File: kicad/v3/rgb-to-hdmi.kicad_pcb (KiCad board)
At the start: 2 copper layers, 65 x 30 mm, 30 parts, among them P1 CONN_02X20, P2 CONN_01X03, P3 CONN_01X06, P4 CONN_01X02, P5 CONN_01X06, P6 CONN_01X02, P7 Conn_01x01, SW1 SW_PUSH, SW2 SW_PUSH, SW3 SW_PUSH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

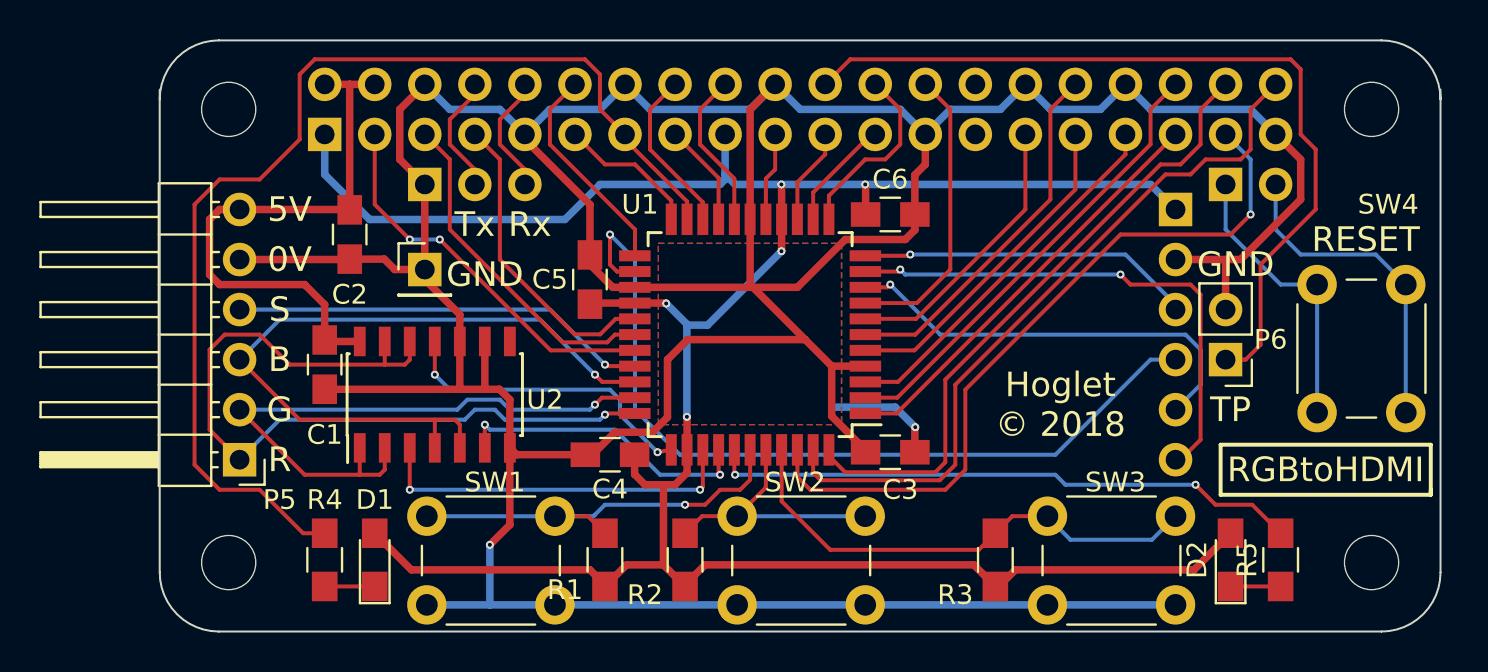
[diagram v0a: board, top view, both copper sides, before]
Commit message: KiCad: corrected via size, cleaned up silk screen
Change-Id: Icce07a46245585d3c723be4bf0025df466743eb7
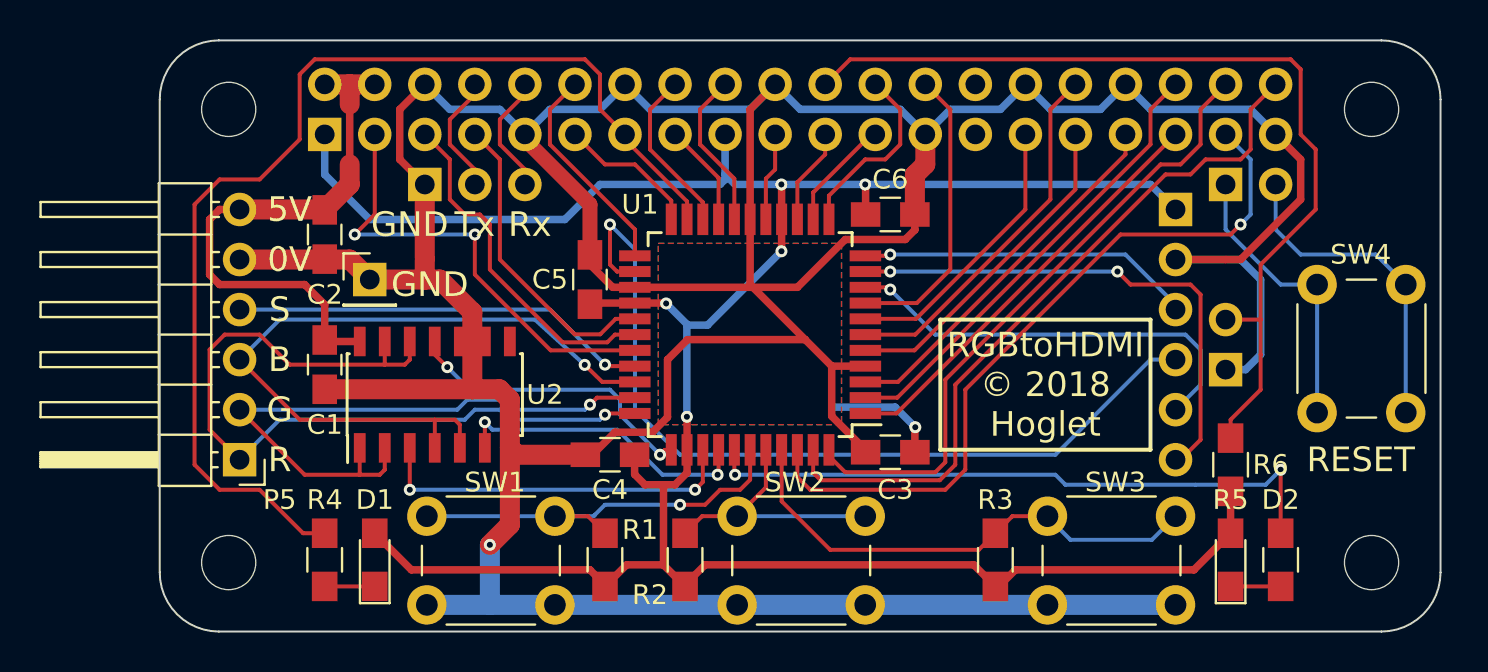
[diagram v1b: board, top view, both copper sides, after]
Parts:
- added R6: 10K, Resistors_SMD:R_0805_HandSoldering, F.Cu at (66.8, 46.0)
- P6: footprint Pin_Headers:Pin_Header_Straight_1x02_Pitch2.54mm -> Pin_Headers:Pin_Header_Angled_1x02_Pitch2.54mm; moved to B.Cu
- moved P7 2.84 mm to (23.2, 36.6)
- moved C2 1.27 mm to (20.9, 34.4)
- moved P6 0.51 mm to (66.6, 41.2), turned to 0 degrees
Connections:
- P6 pad 1: /GPIO25 -> GND
- P6 pad 2: GND -> /GPIO25
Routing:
- net GND: track 227.3 -> 238.1 mm
- net /GPIO25: track 42.4 -> 47.5 mm
- net /GPIO2: track 19.8 -> 23.3 mm
- net /LED: track 30.2 -> 32.7 mm
- net /3V3: track 137.7 -> 139.8 mm
- net /TDO: track 42.7 -> 43.7 mm
- net VCC: track 29.2 -> 28.5 mm
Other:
- outline, holes or cut-outs redrawn
- net class Default: via_dia 0.4064 -> 0.6096; via_drill 0.2032 -> 0.3048
- net class Power: via_dia 0.4064 -> 0.6096; via_drill 0.2032 -> 0.3048
- rule trace_min: 0.1524 -> 0.2032
- rule via_min_drill: 0.2032 -> 0.3048
- rule via_min_size: 0.4064 -> 0.6096
- board text added: "DEBUG"
- board text added: "LINK"
- board text added: "RGBtoHDMI © 2018 Hoglet"
- board text removed: "Hoglet © 2018"
- board text removed: "RGBtoHDMI"
- board text removed: "TP"

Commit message: KiCad: removed SW2/3 passthrough, use gpio 19/26 instead
Change-Id: I88240f36d608d24969d40a8aa7c47a878a85b3d9
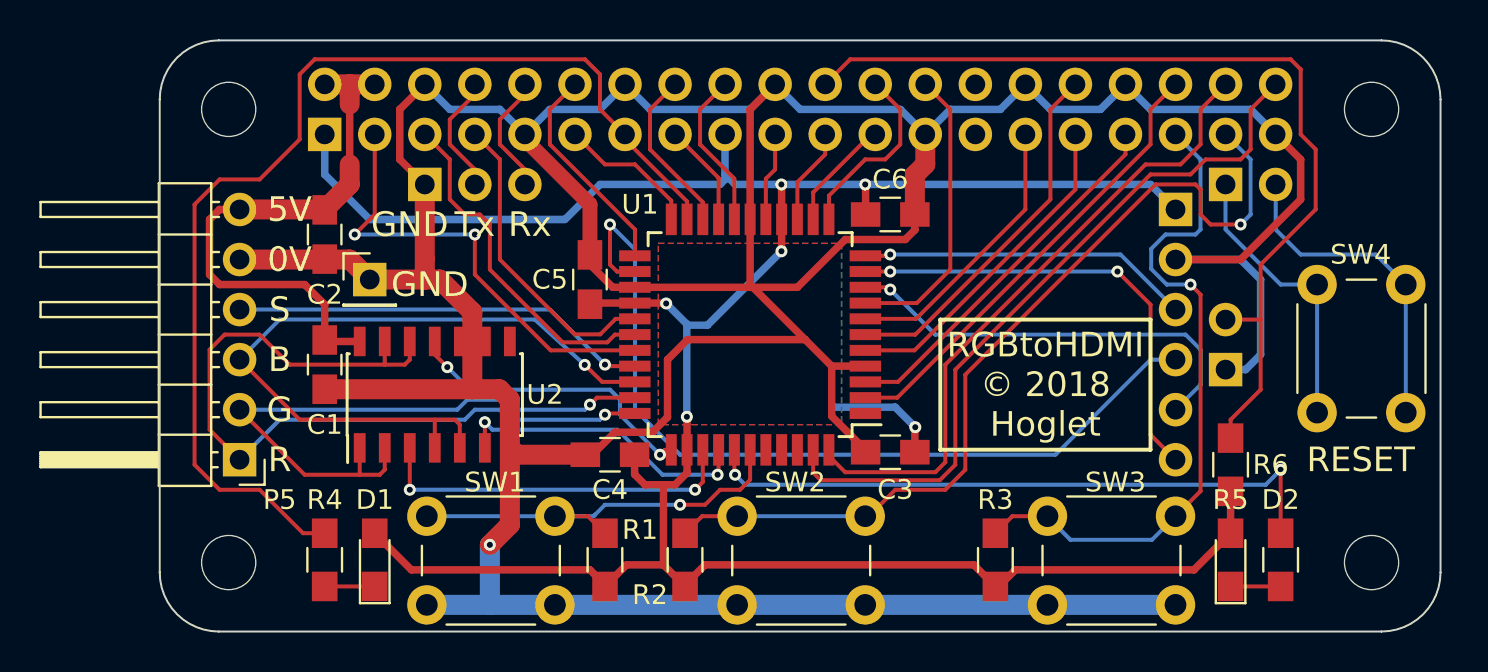
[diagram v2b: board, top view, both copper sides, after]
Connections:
- R2 pad 2: /SW2 -> /GPIO26
- R3 pad 2: /SW3 -> /GPIO19
- SW2 pad 2: /SW2 -> /GPIO26
- SW3 pad 2: /SW3 -> /GPIO19
- U1 pad 1: /GPIO19 -> (no net)
- U1 pad 40: /SW2 -> (no net)
- U1 pad 41: /SW3 -> (no net)
- U1 pad 42: /GPIO26 -> (no net)
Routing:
- net /SW3: track 25.3 -> 0.00 mm
- net /SW2: track 13.5 -> 0.00 mm
- net /GPIO19: track 21.6 -> 34.6 mm, vias 0 -> 1
- net /GPIO26: track 37.4 -> 45.2 mm
- net /TMS: track 26.7 -> 24.0 mm

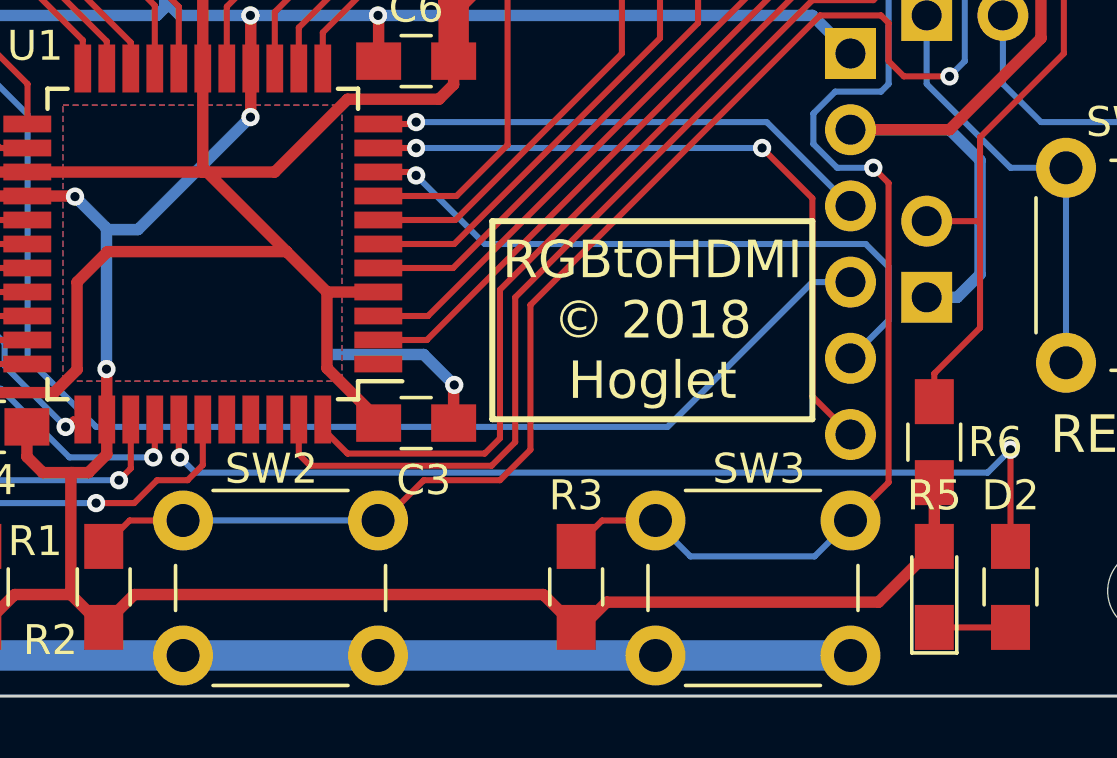
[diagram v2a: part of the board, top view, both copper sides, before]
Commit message: KiCad and CPLD: final small changes to bring SW2/3/link inputs and LED1 output to CPLD (unused)
Change-Id: I054dcab88885547d6ceb07bc2759daf81372ef52
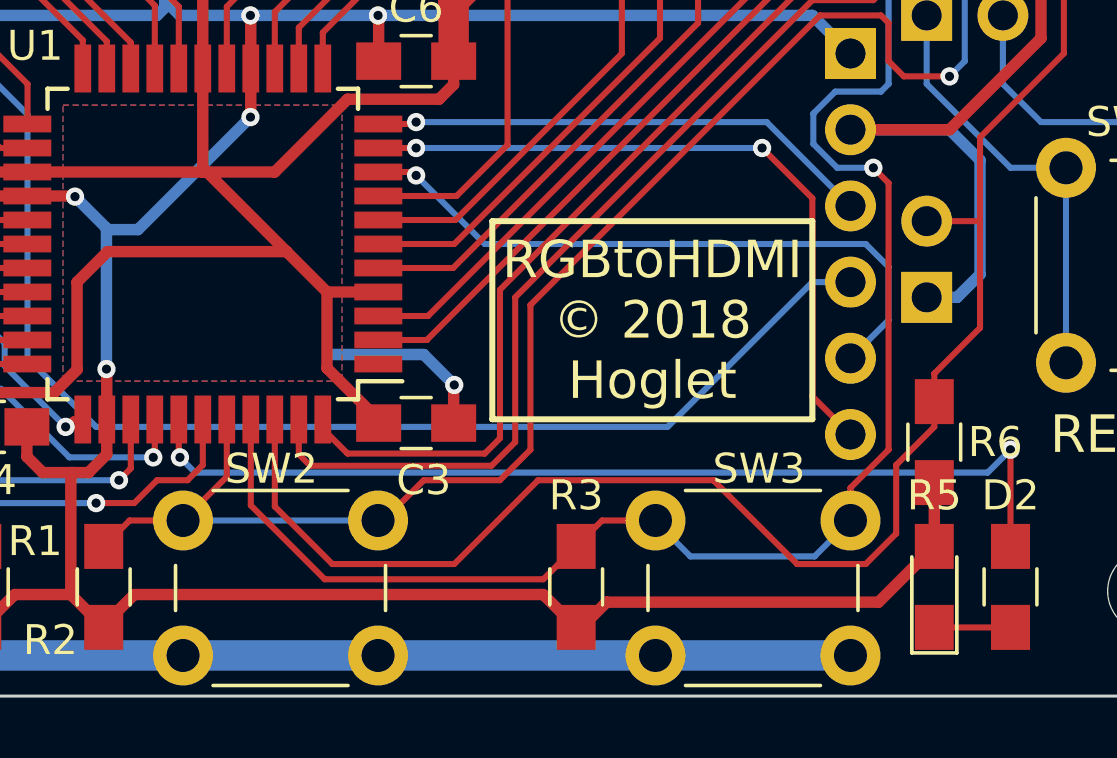
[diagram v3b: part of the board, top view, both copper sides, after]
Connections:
- U1 pad 40: (no net) -> /GPIO26
- U1 pad 41: (no net) -> /GPIO19
- U1 pad 42: (no net) -> /GPIO25
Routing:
- net /GPIO25: track 47.5 -> 79.5 mm
- net /GPIO19: track 34.6 -> 49.8 mm
- net /GPIO26: track 45.2 -> 49.2 mm
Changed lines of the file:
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@@
 (kicad_pcb (version 4) (host pcbnew 4.0.7-e2-6376~58~ubuntu16.04.1)
   (general
-    (links 109)
+    (links 112)
     (no_connects 0)
     (area 12.449999 24.449999 77.550001 54.550001)
     (thickness 1.6)
     (drawings 49)
-    (tracks 513)
+    (tracks 530)
     (zones 0)
     (modules 31)
@@
     (pad 39 smd rect (at 0 -5.85 270) (size 1.6 0.56) (layers F.Cu F.Paste F.Mask)
       (net 39 /SW1))
-    (pad 40 smd rect (at -0.8 -5.85 270) (size 1.6 0.56) (layers F.Cu F.Paste F.Mask))
-    (pad 41 smd rect (at -1.6 -5.85 270) (size 1.6 0.56) (layers F.Cu F.Paste F.Mask))
-    (pad 42 smd rect (at -2.4 -5.85 270) (size 1.6 0.56) (layers F.Cu F.Paste F.Mask))
+    (pad 40 smd rect (at -0.8 -5.85 270) (size 1.6 0.56) (layers F.Cu F.Paste F.Mask)
+      (net 26 /GPIO26))
+    (pad 41 smd rect (at -1.6 -5.85 270) (size 1.6 0.56) (layers F.Cu F.Paste F.Mask)
+      (net 24 /GPIO19))
+    (pad 42 smd rect (at -2.4 -5.85 270) (size 1.6 0.56) (layers F.Cu F.Paste F.Mask)
+      (net 46 /GPIO25))
     (pad 43 smd rect (at -3.2 -5.85 270) (size 1.6 0.56) (layers F.Cu F.Paste F.Mask)
       (net 28 /GPIO21))
@@
   (segment (start 49.968 41.83096) (end 61.512 30.28696) (width 0.2032) (layer F.Cu) (net 23))
   (segment (start 61.512 30.28696) (end 61.512 29.27096) (width 0.2032) (layer F.Cu) (net 23) (status 20))
+  (segment (start 64.052 48.64696) (end 64.052 47.55896) (width 0.2032) (layer F.Cu) (net 24) (status 10))
+  (segment (start 64.052 47.55896) (end 65.322 46.28896) (width 0.2032) (layer F.Cu) (net 24))
+  (segment (start 44.062 45.28096) (end 44.062 48.14296) (width 0.2032) (layer F.Cu) (net 24) (status 10))
+  (segment (start 53.812 50.60696) (end 54.908 49.51096) (width 0.2032) (layer F.Cu) (net 24) (status 20))
+  (segment (start 46.526 50.60696) (end 53.812 50.60696) (width 0.2032) (layer F.Cu) (net 24))
+  (segment (start 44.062 48.14296) (end 46.526 50.60696) (width 0.2032) (layer F.Cu) (net 24))
   (segment (start 64.052 29.27096) (end 65.322 30.54096) (width 0.2032) (layer B.Cu) (net 24) (status 10))
-  (segment (start 65.322 47.37696) (end 64.052 48.64696) (width 0.2032) (layer F.Cu) (net 24) (status 20))
-  (segment (start 65.322 37.39896) (end 65.322 47.37696) (width 0.2032) (layer F.Cu) (net 24))
+  (segment (start 65.322 30.54096) (end 65.322 34.09696) (width 0.2032) (layer B.Cu) (net 24))
+  (segment (start 65.322 34.09696) (end 65.068 34.35096) (width 0.2032) (layer B.Cu) (net 24))
+  (segment (start 65.068 34.35096) (end 63.544 34.35096) (width 0.2032) (layer B.Cu) (net 24))
+  (segment (start 63.544 34.35096) (end 62.81537 35.07959) (width 0.2032) (layer B.Cu) (net 24))
+  (segment (start 62.81537 35.07959) (end 62.81537 36.09559) (width 0.2032) (layer B.Cu) (net 24))
+  (segment (start 62.81537 36.09559) (end 63.61074 36.89096) (width 0.2032) (layer B.Cu) (net 24))
+  (segment (start 63.61074 36.89096) (end 64.814 36.89096) (width 0.2032) (layer B.Cu) (net 24))
+  (via (at 64.814 36.89096) (size 0.6096) (drill 0.3048) (layers F.Cu B.Cu) (net 24))
   (segment (start 64.814 36.89096) (end 65.322 37.39896) (width 0.2032) (layer F.Cu) (net 24))
-  (via (at 64.814 36.89096) (size 0.6096) (drill 0.3048) (layers F.Cu B.Cu) (net 24))
-  (segment (start 63.61074 36.89096) (end 64.814 36.89096) (width 0.2032) (layer B.Cu) (net 24))
-  (segment (start 62.81537 36.09559) (end 63.61074 36.89096) (width 0.2032) (layer B.Cu) (net 24))
-  (segment (start 62.81537 35.07959) (end 62.81537 36.09559) (width 0.2032) (layer B.Cu) (net 24))
-  (segment (start 63.544 34.35096) (end 62.81537 35.07959) (width 0.2032) (layer B.Cu) (net 24))
-  (segment (start 65.068 34.35096) (end 63.544 34.35096) (width 0.2032) (layer B.Cu) (net 24))
-  (segment (start 65.322 34.09696) (end 65.068 34.35096) (width 0.2032) (layer B.Cu) (net 24))
-  (segment (start 65.322 30.54096) (end 65.322 34.09696) (width 0.2032) (layer B.Cu) (net 24))
+  (segment (start 65.322 37.39896) (end 65.322 46.28896) (width 0.2032) (layer F.Cu) (net 24))
   (segment (start 57.552 48.64696) (end 57.552 48.67896) (width 0.2032) (layer B.Cu) (net 24) (status 30))
   (segment (start 57.552 48.67896) (end 58.718 49.84496) (width 0.2032) (layer B.Cu) (net 24) (status 10))
@@
   (segment (start 62.782 29.77896) (end 62.782 28.00096) (width 0.2032) (layer F.Cu) (net 25))
   (segment (start 49.93 42.63096) (end 62.782 29.77896) (width 0.2032) (layer F.Cu) (net 25))
+  (segment (start 43.262 45.28096) (end 43.262 47.18896) (width 0.2032) (layer F.Cu) (net 26) (status 10))
+  (segment (start 43.262 47.18896) (end 41.804 48.64696) (width 0.2032) (layer F.Cu) (net 26) (status 20))
   (segment (start 53.384 41.46296) (end 63.036 31.81096) (width 0.2032) (layer F.Cu) (net 26))
   (segment (start 65.83 33.84296) (end 67.354 33.84296) (width 0.2032) (layer F.Cu) (net 26))
@@
   (segment (start 42.208 47.05096) (end 68.624 47.05096) (width 0.2032) (layer B.Cu) (net 45))
   (segment (start 41.7 46.54296) (end 42.208 47.05096) (width 0.2032) (layer B.Cu) (net 45))
-  (segment (start 41.7 46.54296) (end 41.7 46.54296) (width 0.2032) (layer B.Cu) (net 45))
   (via (at 41.7 46.54296) (size 0.6096) (drill 0.3048) (layers F.Cu B.Cu) (net 45))
   (segment (start 41.662 46.50496) (end 41.7 46.54296) (width 0.2032) (layer F.Cu) (net 45))
@@
   (via (at 69.386 46.28896) (size 0.6096) (drill 0.3048) (layers F.Cu B.Cu) (net 45))
   (segment (start 68.624 47.05096) (end 69.386 46.28896) (width 0.2032) (layer B.Cu) (net 45))
+  (segment (start 66.846 45.52696) (end 65.576 46.79696) (width 0.2032) (layer F.Cu) (net 46))
+  (segment (start 65.576 46.79696) (end 65.576 49.08296) (width 0.2032) (layer F.Cu) (net 46))
+  (segment (start 65.576 49.08296) (end 64.56 50.09896) (width 0.2032) (layer F.Cu) (net 46))
+  (segment (start 64.56 50.09896) (end 62.274 50.09896) (width 0.2032) (layer F.Cu) (net 46))
+  (segment (start 62.274 50.09896) (end 59.48 47.30496) (width 0.2032) (layer F.Cu) (net 46))
+  (segment (start 59.48 47.30496) (end 53.638 47.30496) (width 0.2032) (layer F.Cu) (net 46))
+  (segment (start 53.638 47.30496) (end 50.844 50.09896) (width 0.2032) (layer F.Cu) (net 46))
+  (segment (start 50.844 50.09896) (end 46.78 50.09896) (width 0.2032) (layer F.Cu) (net 46))
+  (segment (start 66.846 44.68496) (end 66.846 45.52696) (width 0.2032) (layer F.Cu) (net 46) (status 10))
+  (segment (start 44.862 48.18096) (end 44.862 45.28096) (width 0.2032) (layer F.Cu) (net 46) (status 20))
+  (segment (start 46.78 50.09896) (end 44.862 48.18096) (width 0.2032) (layer F.Cu) (net 46))
   (segment (start 66.592 38.66896) (end 68.37 38.66896) (width 0.2032) (layer F.Cu) (net 46) (status 10))
   (segment (start 66.846 44.68496) (end 66.846 43.74896) (width 0.2032) (layer F.Cu) (net 46) (status 10))
